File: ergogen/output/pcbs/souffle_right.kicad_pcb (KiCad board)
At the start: 2 copper layers, 138.1 x 117.1 mm, 60 parts

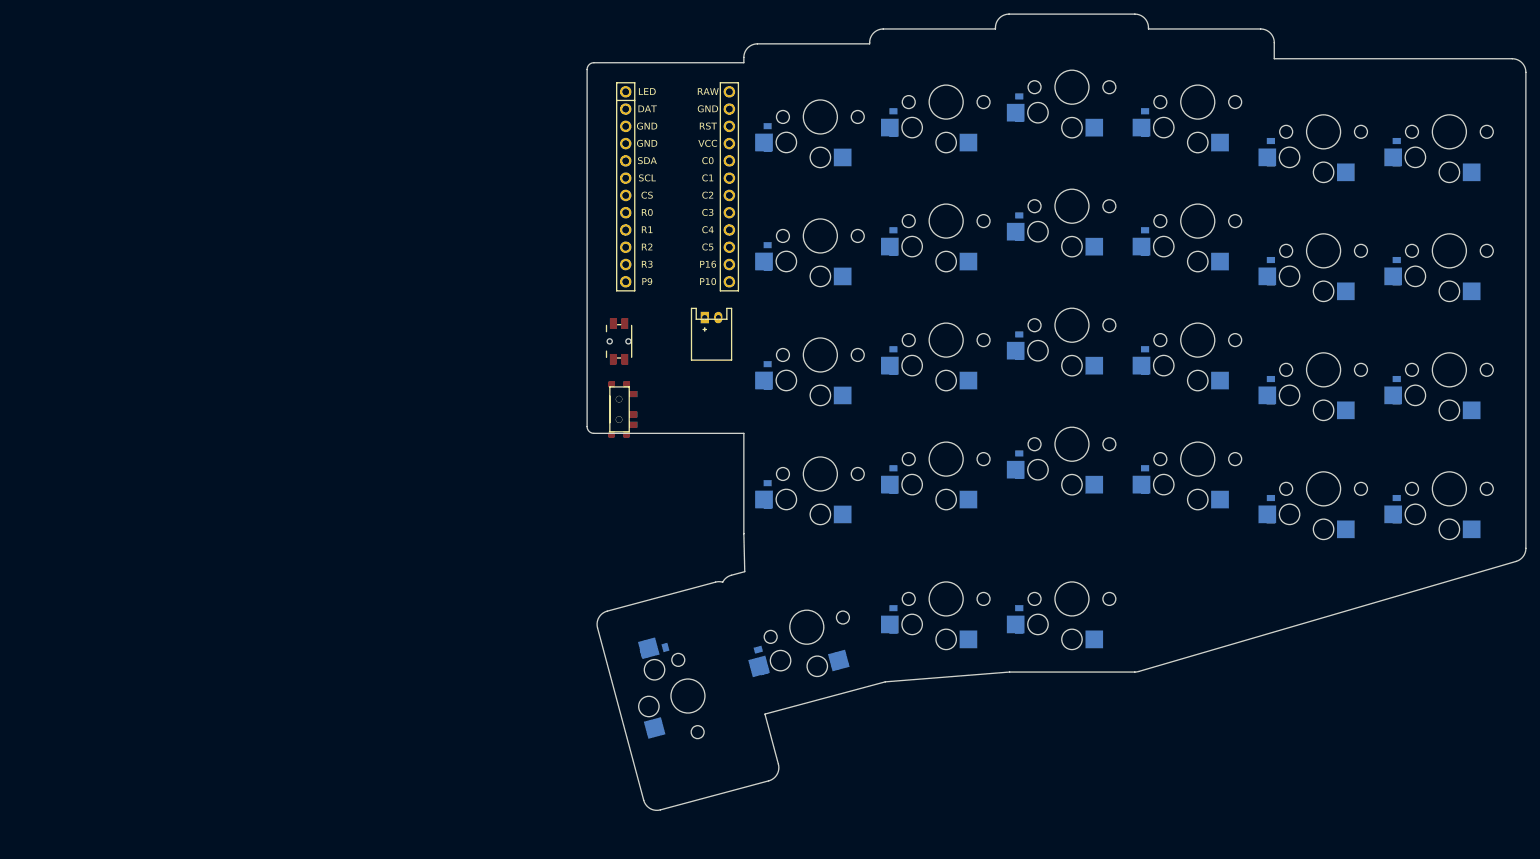
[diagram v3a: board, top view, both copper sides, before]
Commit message: feat: mcu and buttons positioning for the right hand
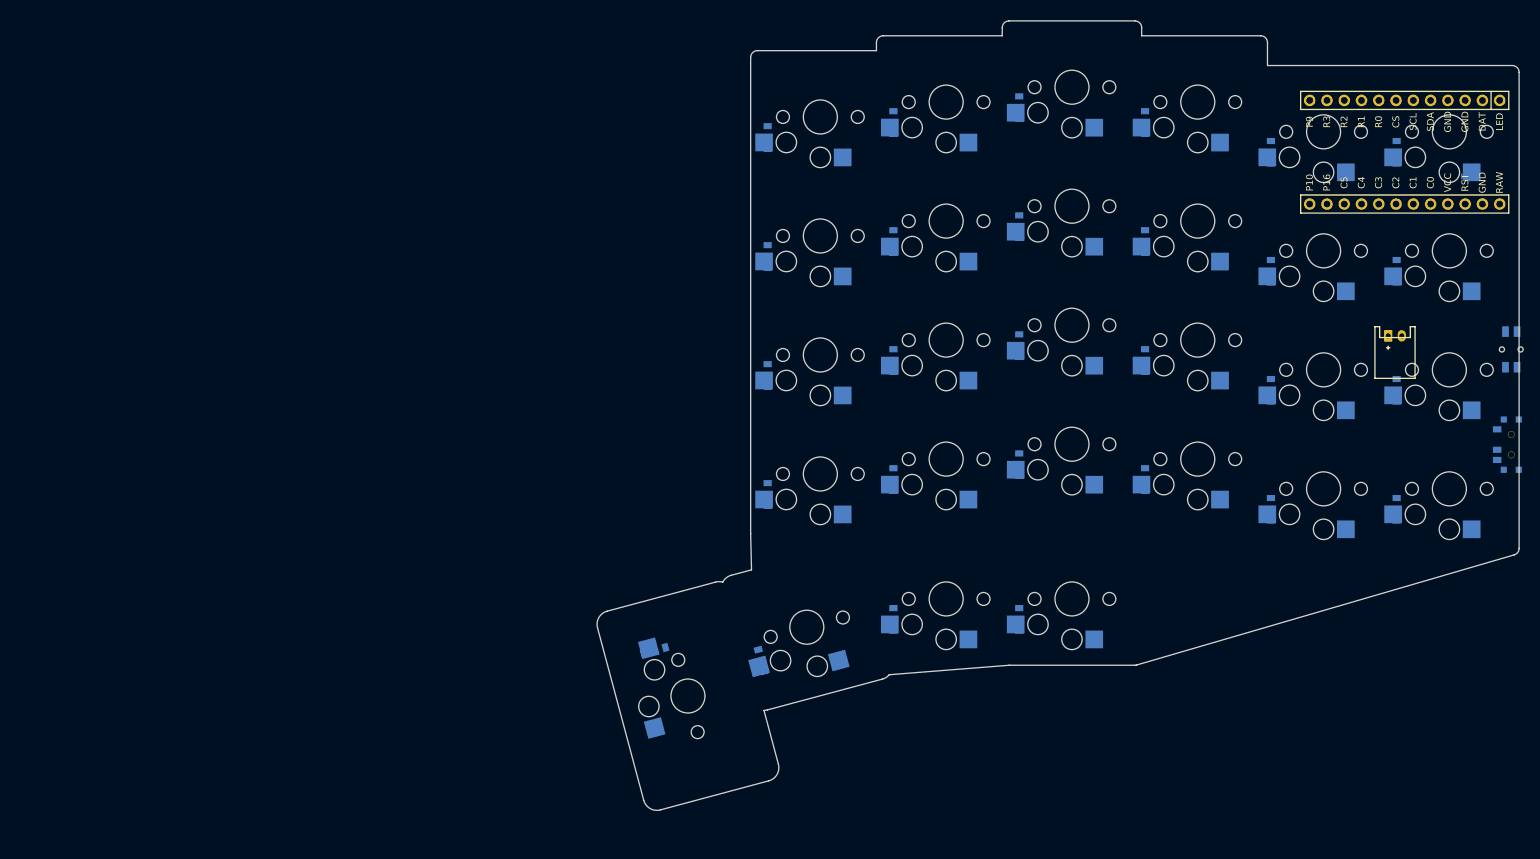
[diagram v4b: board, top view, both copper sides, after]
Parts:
- moved T1 131.3 mm to (374.1, 93.5), turned to -90 degrees
- moved B1 131.2 mm to (374.1, 79.5), turned to -90 degrees
- moved MCU1 108.3 mm to (359.7, 50.5), turned to -90 degrees
- moved JST1 100.5 mm to (357.0, 77.5)
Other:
- board size 138.1 x 117.1 mm -> 135.6 x 116.1 mm

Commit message: feat: left hand redesign
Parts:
- removed D28: , ceoloide:diode_tht_sod123
- removed S28: , ceoloide:switch_choc_v1_v2
- added MH1: , ceoloide:mounting_hole_npth, F.Cu at (337.3, 36.4)
- added MH2: , ceoloide:mounting_hole_npth, F.Cu at (263.0, 49.8)
- added MH3: , ceoloide:mounting_hole_npth, F.Cu at (374.2, 131.2)
- added MH4: , ceoloide:mounting_hole_npth, F.Cu at (261.2, 126.9)
- S1, S10, S11, S12, S13, S14, S15, S16, S17, S18, S19, S2, S20, S21, S22, S23, S24, S25, S26, S27, S3, S4, S5, S6, S7, S8, S9: footprint ceoloide:switch_choc_v1_v2 -> CPG1316S01D02_mikeholscher; moved to F.Cu
- moved MCU1 108.4 mm to (253.0, 69.4), turned to 0 degrees
- moved S26 22.5 mm to (281.9, 136.7), turned to 7.5 degrees
- moved S25 21.6 mm to (300.2, 135.7), turned to 0 degrees
- moved S27 20.8 mm to (263.9, 140.1), turned to 15 degrees
- moved S1 20.0 mm to (365.0, 120.0), turned to 0 degrees
- moved S5 20.0 mm to (346.5, 120.0), turned to 0 degrees
- moved S21 19.9 mm to (272.5, 117.7), turned to 0 degrees
- moved S17 19.8 mm to (291.0, 115.4), turned to 0 degrees
- moved S9 19.8 mm to (328.0, 115.4), turned to 0 degrees
- moved S13 19.6 mm to (309.5, 113.1), turned to 0 degrees
- moved D26 19.4 mm to (274.0, 136.2), turned to -82.5 degrees
- moved B1 19.0 mm to (374.1, 98.5)
- moved JST1 19.0 mm to (357.0, 96.5)
- moved S2 19.0 mm to (365.0, 101.5), turned to 0 degrees
- moved S6 19.0 mm to (346.5, 101.5), turned to 0 degrees
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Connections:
- D26 pad 2: mirror_outward_home -> mirror_middle_home
- D27 pad 2: mirror_small_thumbkey_home -> mirror_outward_home
- S1 pad 1: C0 -> mirror_outer_bottom
- S1 pad 2: mirror_outer_bottom -> C0
- S10 pad 1: C2 -> mirror_ring_home
- S10 pad 2: mirror_ring_home -> C2
- S11 pad 1: C2 -> mirror_ring_top
- S11 pad 2: mirror_ring_top -> C2
- S12 pad 1: C2 -> mirror_ring_number
- S12 pad 2: mirror_ring_number -> C2
- S13 pad 1: C3 -> mirror_middle_bottom
- S13 pad 2: mirror_middle_bottom -> C3
- S14 pad 1: C3 -> mirror_middle_home
- S14 pad 2: mirror_middle_home -> C3
- S15 pad 1: C3 -> mirror_middle_top
- S15 pad 2: mirror_middle_top -> C3
- S16 pad 1: C3 -> mirror_middle_number
- S16 pad 2: mirror_middle_number -> C3
- S17 pad 1: C4 -> mirror_index_bottom
- S17 pad 2: mirror_index_bottom -> C4
- S18 pad 1: C4 -> mirror_index_home
- S18 pad 2: mirror_index_home -> C4
- S19 pad 1: C4 -> mirror_index_top
- S19 pad 2: mirror_index_top -> C4
- S2 pad 1: C0 -> mirror_outer_home
- S2 pad 2: mirror_outer_home -> C0
- S20 pad 1: C4 -> mirror_index_number
- S20 pad 2: mirror_index_number -> C4
- S21 pad 1: C5 -> mirror_inner_bottom
- S21 pad 2: mirror_inner_bottom -> C5
- S22 pad 1: C5 -> mirror_inner_home
- S22 pad 2: mirror_inner_home -> C5
- S23 pad 1: C5 -> mirror_inner_top
- S23 pad 2: mirror_inner_top -> C5
- S24 pad 1: C5 -> mirror_inner_number
- S24 pad 2: mirror_inner_number -> C5
- S25 pad 1: C2 -> mirror_inward_home
- S25 pad 2: mirror_inward_home -> C2
- S26 pad 1: C3 -> mirror_middle_home
- S26 pad 2: mirror_outward_home -> C4
- S27 pad 1: C4 -> mirror_outward_home
- S27 pad 2: mirror_small_thumbkey_home -> C5
- S3 pad 1: C0 -> mirror_outer_top
- S3 pad 2: mirror_outer_top -> C0
- S4 pad 1: C0 -> mirror_outer_number
- S4 pad 2: mirror_outer_number -> C0
- S5 pad 1: C1 -> mirror_pinky_bottom
- S5 pad 2: mirror_pinky_bottom -> C1
- S6 pad 1: C1 -> mirror_pinky_home
- S6 pad 2: mirror_pinky_home -> C1
- S7 pad 1: C1 -> mirror_pinky_top
- S7 pad 2: mirror_pinky_top -> C1
- S8 pad 1: C1 -> mirror_pinky_number
- S8 pad 2: mirror_pinky_number -> C1
- S9 pad 1: C2 -> mirror_ring_bottom
- S9 pad 2: mirror_ring_bottom -> C2
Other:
- board size 135.6 x 116.1 mm -> 132.5 x 105.1 mm

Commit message: feat: attempt to move mcu to bottom
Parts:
- S1, S10, S11, S12, S13, S14, S15, S16, S17, S18, S19, S2, S20, S21, S22, S23, S24, S25, S26, S27, S3, S4, S5, S6, S7, S8, S9: footprint CPG1316S01D02_mikeholscher -> CPG1316S01D02
- moved JST1 201.9 mm to (156.9, 123.5)
- moved MH1 101.4 mm to (308.1, 133.5)
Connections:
- S1 pad 1: mirror_outer_bottom -> C0
- S1 pad 2: C0 -> mirror_outer_bottom
- S10 pad 1: mirror_ring_home -> C2
- S10 pad 2: C2 -> mirror_ring_home
- S11 pad 1: mirror_ring_top -> C2
- S11 pad 2: C2 -> mirror_ring_top
- S12 pad 1: mirror_ring_number -> C2
- S12 pad 2: C2 -> mirror_ring_number
- S13 pad 1: mirror_middle_bottom -> C3
- S13 pad 2: C3 -> mirror_middle_bottom
- S14 pad 1: mirror_middle_home -> C3
- S14 pad 2: C3 -> mirror_middle_home
- S15 pad 1: mirror_middle_top -> C3
- S15 pad 2: C3 -> mirror_middle_top
- S16 pad 1: mirror_middle_number -> C3
- S16 pad 2: C3 -> mirror_middle_number
- S17 pad 1: mirror_index_bottom -> C4
- S17 pad 2: C4 -> mirror_index_bottom
- S18 pad 1: mirror_index_home -> C4
- S18 pad 2: C4 -> mirror_index_home
- S19 pad 1: mirror_index_top -> C4
- S19 pad 2: C4 -> mirror_index_top
- S2 pad 1: mirror_outer_home -> C0
- S2 pad 2: C0 -> mirror_outer_home
- S20 pad 1: mirror_index_number -> C4
- S20 pad 2: C4 -> mirror_index_number
- S21 pad 1: mirror_inner_bottom -> C5
- S21 pad 2: C5 -> mirror_inner_bottom
- S22 pad 1: mirror_inner_home -> C5
- S22 pad 2: C5 -> mirror_inner_home
- S23 pad 1: mirror_inner_top -> C5
- S23 pad 2: C5 -> mirror_inner_top
- S24 pad 1: mirror_inner_number -> C5
- S24 pad 2: C5 -> mirror_inner_number
- S25 pad 1: mirror_inward_home -> C3
- S25 pad 2: C2 -> mirror_inward_home
- S26 pad 1: mirror_middle_home -> C4
- S26 pad 2: C4 -> mirror_middle_home
- S27 pad 1: mirror_outward_home -> C5
- S27 pad 2: C5 -> mirror_outward_home
- S3 pad 1: mirror_outer_top -> C0
- S3 pad 2: C0 -> mirror_outer_top
- S4 pad 1: mirror_outer_number -> C0
- S4 pad 2: C0 -> mirror_outer_number
- S5 pad 1: mirror_pinky_bottom -> C1
- S5 pad 2: C1 -> mirror_pinky_bottom
- S6 pad 1: mirror_pinky_home -> C1
- S6 pad 2: C1 -> mirror_pinky_home
- S7 pad 1: mirror_pinky_top -> C1
- S7 pad 2: C1 -> mirror_pinky_top
- S8 pad 1: mirror_pinky_number -> C1
- S8 pad 2: C1 -> mirror_pinky_number
- S9 pad 1: mirror_ring_bottom -> C2
- S9 pad 2: C2 -> mirror_ring_bottom
